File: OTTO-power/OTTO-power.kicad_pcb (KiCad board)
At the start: 2 copper layers, 72.5 x 23.5 mm, 47 parts, among them J1 Barrel_Jack, J2 Conn_01x10, J3 USB_B_Micro, J4 battery, SW1 SW_Push, U1 MAX8903A, U2 MAX17048, U3 TPS61090, U4 XC6210

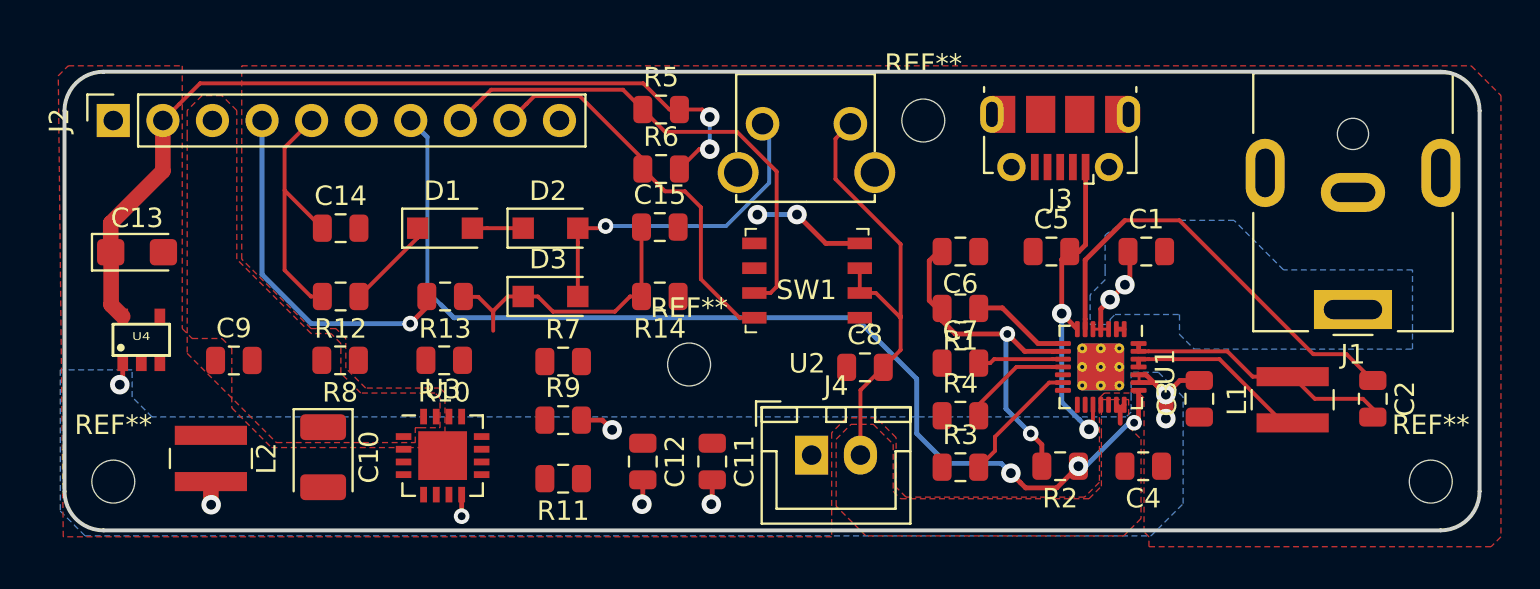
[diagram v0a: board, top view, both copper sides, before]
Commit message: Revert "Revert "added a reset button to the power board""
This reverts commit f20825db904c66ff1a5b44b22e19a70ce58abb56.
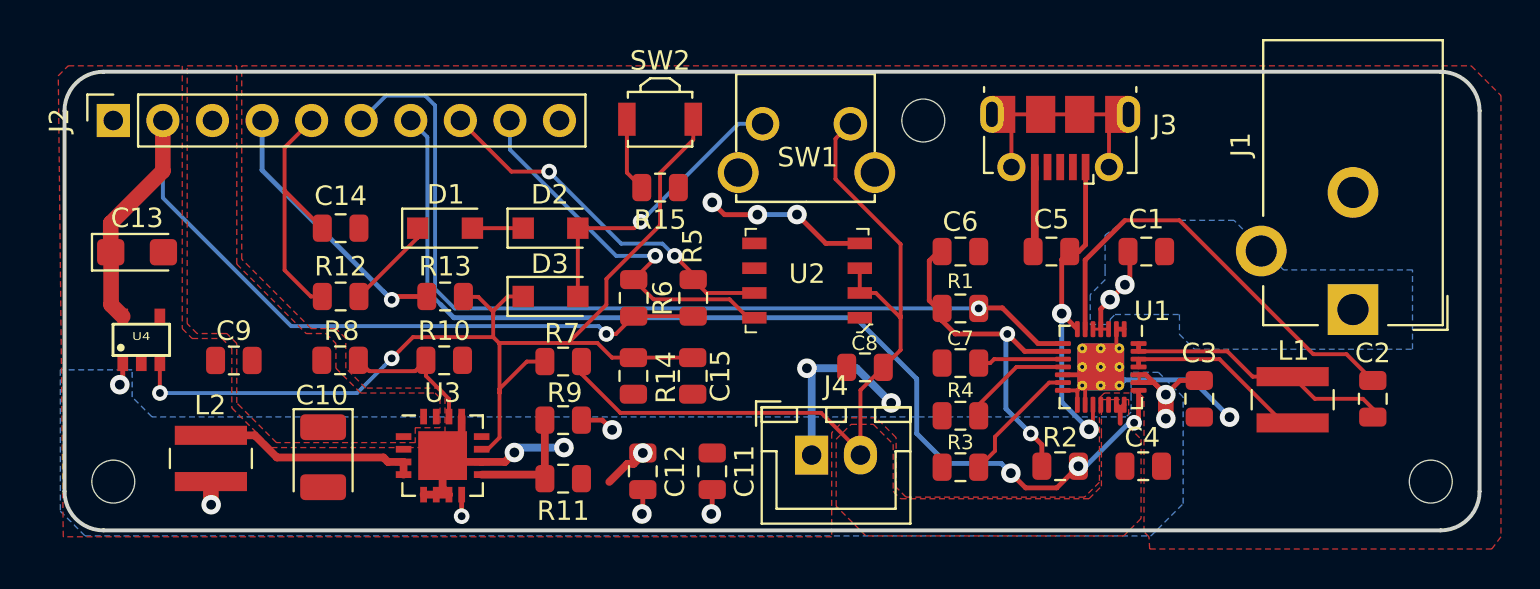
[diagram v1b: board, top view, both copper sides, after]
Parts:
- removed the REF** at (181.5, 38.8)
- added R15: 1K, Resistor_SMD:R_0805_2012Metric, F.Cu at (180.0, 29.8)
- added SW2: SW_reset, Button_Switch_SMD:SW_SPST_B3U-3000P, F.Cu at (180.0, 26.2)
- C14: value 0.1uF -> 0.1uf
- C15: value 0.1uF -> 100uf
- J1: footprint Connector_BarrelJack:BarrelJack_CUI_PJ-063AH_Horizontal -> Connector_BarrelJack:BarrelJack_CUI_PJ-102AH_Horizontal
- R14: value 10K -> 100K
- moved R5 9.79 mm to (181.7, 35.4), turned to 270 degrees
- moved C15 7.81 mm to (181.7, 39.4), turned to 270 degrees
- moved R6 6.75 mm to (178.6, 35.4), turned to 270 degrees
- moved R14 4.29 mm to (178.6, 39.4), turned to 90 degrees
- moved C11 0.50 mm to (182.7, 44.3)
- moved C12 0.50 mm to (179.1, 44.3)
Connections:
- J3 pad 2: Net-(J3-Pad2) -> (no net)
- J3 pad 3: Net-(J3-Pad3) -> (no net)
- J3 pad 4: Net-(J3-Pad4) -> (no net)
- U1 pad 18: Net-(U1-Pad18) -> (no net)
- U1 pad 19: Net-(U1-Pad19) -> (no net)
- U1 pad 29: (no net) -> GNDA
- U2 pad 5: Net-(U2-Pad5) -> (no net)
- U3 pad 12: Net-(U3-Pad12) -> (no net)
- U3 pad 2: Net-(U3-Pad2) -> (no net)
- U4 pad 4: Net-(U4-Pad4) -> (no net)
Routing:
- net GNDA: track 6.84 -> 52.6 mm, vias 2 -> 9
- net EN_PI: track 15.2 -> 59.5 mm, vias 0 -> 2
- net DOK_OUT: track 5.08 -> 47.3 mm, vias 0 -> 1
- net BATT+: track 25.0 -> 41.8 mm
- net Net-(J3-Pad6): track 0.00 -> 13.6 mm
- net Net-(L2-Pad1): track 0.00 -> 11.1 mm
- net Net-(R10-Pad2): track 0.00 -> 7.29 mm
- net SCL: track 25.8 -> 18.9 mm, vias 0 -> 2
- net Net-(R11-Pad2): track 0.00 -> 6.32 mm
- net OUT_PIN: track 18.3 -> 13.8 mm
- net Net-(R15-Pad2): track 0.00 -> 3.82 mm
- net Net-(D2-Pad2): track 17.8 -> 15.5 mm
- net 3V3: track 44.5 -> 45.8 mm, vias 2 -> 1
- net SDA: track 20.2 -> 19.9 mm, vias 0 -> 1

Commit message: progresses in the mainboard wiring
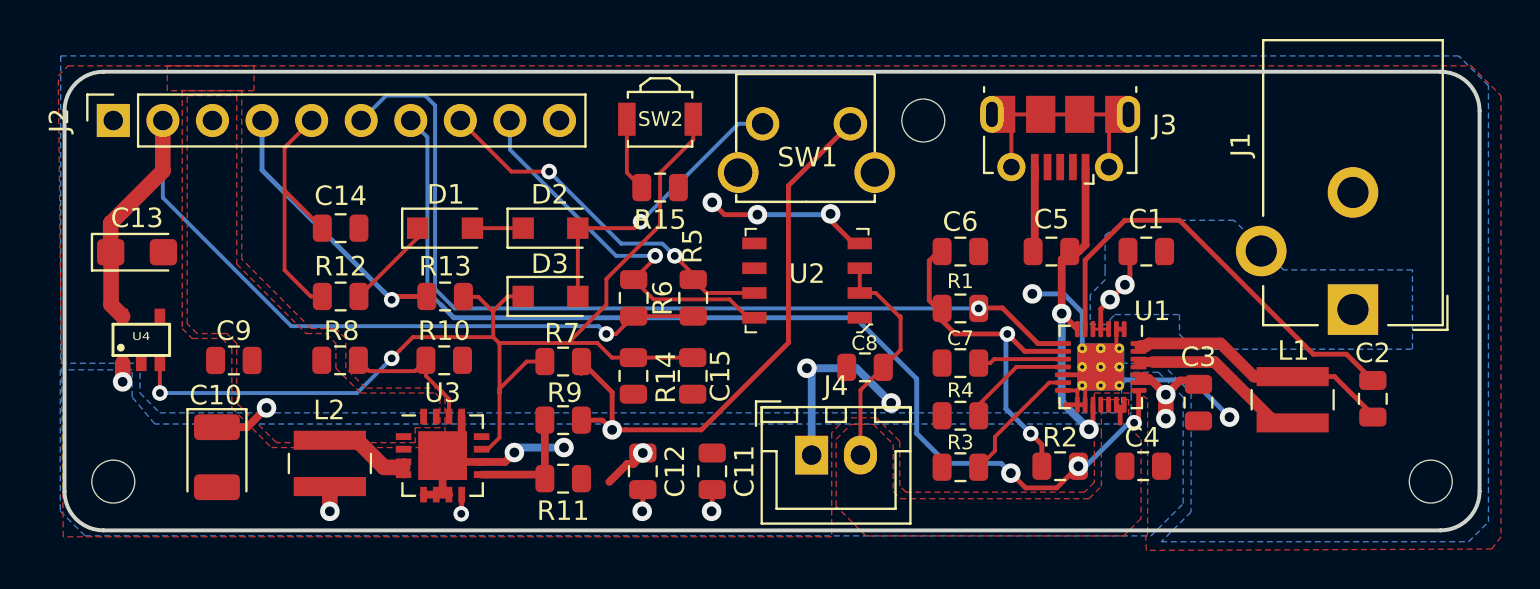
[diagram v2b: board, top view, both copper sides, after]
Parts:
- moved L2 6.10 mm to (163.1, 43.9)
- moved C10 5.44 mm to (157.3, 43.6)
- moved C3 0.20 mm to (207.6, 40.8)
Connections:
- R7 pad 2: BATT+ -> SYS
- SW1 pad 1: BATT+ -> SYS
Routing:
- net BATT+: track 41.8 -> 13.5 mm
- net SYS: track 14.9 -> 43.1 mm
- net Net-(L2-Pad1): track 11.1 -> 4.96 mm
- net GNDA: track 52.6 -> 58.7 mm, vias 9 -> 10
- net 5V: track 0.00 -> 2.95 mm, vias 0 -> 1
- added copper zone on B.Cu, net GNDA
